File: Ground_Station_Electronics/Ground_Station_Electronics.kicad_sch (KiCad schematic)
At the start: 32 parts

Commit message: "done" but ugly
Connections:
- net SRV1_PWM: now also U2.5 (P3); no longer U2.4 (P2)
- net SRV2_PWM: now also U2.4 (P2); no longer U2.5 (P3)
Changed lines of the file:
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@@
     (effects (font (size 1.27 1.27)) (justify right bottom))
   )
-  (label "SRV1_PWM" (at 63.5 48.26 180)
+  (label "SRV1_PWM" (at 63.5 50.8 180)
     (effects (font (size 1.27 1.27)) (justify right bottom))
   )
@@
     (effects (font (size 1.27 1.27)) (justify left bottom))
   )
-  (label "SRV2_PWM" (at 63.5 50.8 180)
+  (label "SRV2_PWM" (at 63.5 48.26 180)
     (effects (font (size 1.27 1.27)) (justify right bottom))
   )

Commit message: Working on PCB
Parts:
- added H1, H2, H3: MountingHole_Pad, MountingHole:MountingHole_3.2mm_M3_Pad, symbol Mechanical:MountingHole_Pad
- added H4: (no value), symbol Mechanical:MountingHole_Pad
- added J?: (no value), symbol ASTRA_Library:QWIIC_Generic_Conn
- BT1: value (none) -> DNP; footprint (none) -> Connector_AMASS:AMASS_XT30U-M_1x02_P5.0mm_Vertical
- C1, C3: value (none) -> 100u; footprint (none) -> Capacitor_SMD:CP_Elec_10x10
- C2, C5: value (none) -> 1m; footprint (none) -> Capacitor_THT:C_Radial_D10.0mm_H12.5mm_P5.00mm
- C4, C6: value (none) -> 100n; footprint (none) -> Capacitor_SMD:C_0603_1608Metric
- D1, D2, D3: value (none) -> G; footprint (none) -> LED_SMD:LED_0603_1608Metric_Pad1.05x0.95mm_HandSolder
- D4: value (none) -> D_Zener; footprint (none) -> Diode_SMD:D_SMB_Handsoldering
- D5: value (none) -> D_Schottky; footprint (none) -> Diode_SMD:D_SMC_Handsoldering
- F1: value (none) -> Polyfuse; footprint (none) -> Fuse:Fuse_2920_7451Metric_Pad2.10x5.45mm_HandSolder
- J1: value (none) -> RJ45_Shielded_Labelled; footprint (none) -> Connector_RJ:RJ45_Amphenol_RJHSE5380
- J2: value (none) -> ARGB_Header; footprint (none) -> Connector_JST:JST_PH_B3B-PH-K_1x03_P2.00mm_Vertical
- L1: value (none) -> L; footprint (none) -> GS_Library:L_Wuerth_HCF-2920
- M1, M2: value (none) -> Motor_Servo; footprint (none) -> Connector_PinHeader_2.54mm:PinHeader_1x03_P2.54mm_Vertical
- R1: value (none) -> 10; footprint (none) -> Resistor_SMD:R_0603_1608Metric
- R2: value (none) -> 180; footprint (none) -> Resistor_SMD:R_0603_1608Metric
- R3: value (none) -> 3.3k; footprint (none) -> Resistor_SMD:R_0603_1608Metric
- R4, R5: value (none) -> 10k; footprint (none) -> Resistor_SMD:R_0603_1608Metric
- R6, R7: value (none) -> 120; footprint (none) -> Resistor_SMD:R_0603_1608Metric
- U1: value (none) -> LM2576HVS-5; footprint (none) -> Package_TO_SOT_SMD:TO-263-5_TabPin3
- U2: value (none) -> Teensy_4.1; footprint (none) -> ASTRA_Footprints:Teensy4.1
- U3: value (none) -> Adafruit_GPS_V3; footprint (none) -> ASTRA_Footprints:Adafruit_GPS_Breakout
- U4: value (none) -> BNO055_Adafruit_Breakout; footprint (none) -> GS_Library:Adafruit_BNO055
- U5: value (none) -> RFM95W_Adafruit_Breakout; footprint (none) -> ASTRA_Footprints:Adafruit_RFM95W
- U6: value (none) -> MAX3488E; footprint (none) -> Package_SO:SOIC-8_3.9x4.9mm_P1.27mm
- U7: value (none) -> SN74AHCT125D; footprint (none) -> Package_SO:SOIC-14_3.9x8.7mm_P1.27mm
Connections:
- net +3V3: now also J?.2 (3.3V)
- net GND: now also J?.1 (GND)
- net SCL: now also J?.4 (SCL)
- net SDA: now also J?.3 (SDA)

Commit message: schematic save
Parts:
- gave numbers to parts that had none: 1
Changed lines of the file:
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@@
   (symbol (lib_id "power:GND") (at 248.92 88.9 0) (unit 1)
     (in_bom yes) (on_board yes) (fields_autoplaced)
-    (property "Reference" "#PWR?" (id 0) (at 248.92 95.25 0)
+    (property "Reference" "#PWR042" (id 0) (at 248.92 95.25 0)
       (effects (font (size 1.27 1.27)) hide)
     )
@@
   (symbol (lib_id "ASTRA_Library:QWIIC_Generic_Conn") (at 265.43 76.2 0) (unit 1)
     (in_bom yes) (on_board yes) (fields_autoplaced)
-    (property "Reference" "J?" (id 0) (at 269.875 82.9853 0)
+    (property "Reference" "J3" (id 0) (at 269.875 82.9853 0)
       (effects (font (size 1.27 1.27)) (justify left))
     )
@@
   (symbol (lib_id "power:+3.3V") (at 248.92 83.82 0) (unit 1)
     (in_bom yes) (on_board yes) (fields_autoplaced)
-    (property "Reference" "#PWR?" (id 0) (at 248.92 87.63 0)
+    (property "Reference" "#PWR041" (id 0) (at 248.92 87.63 0)
       (effects (font (size 1.27 1.27)) hide)
     )
@@
       (reference "#PWR040") (unit 1) (value "GND") (footprint "")
     )
+    (path "/e92f955a-c3b1-473b-96e0-f304b4f9b568"
+      (reference "#PWR041") (unit 1) (value "+3.3V") (footprint "")
+    )
     (path "/d301b315-959a-46e3-9750-4508835fd0e1"
-      (reference "#PWR?") (unit 1) (value "GND") (footprint "")
-    )
-    (path "/e92f955a-c3b1-473b-96e0-f304b4f9b568"
-      (reference "#PWR?") (unit 1) (value "+3.3V") (footprint "")
+      (reference "#PWR042") (unit 1) (value "GND") (footprint "")
     )
     (path "/9e09a5b2-d433-4c89-b155-f02df3929600"
@@
     )
     (path "/dd409643-2ad0-46ca-8edc-7618874343d8"
-      (reference "J?") (unit 1) (value "QWIIC_Generic_Conn") (footprint "")
+      (reference "J3") (unit 1) (value "QWIIC_Generic_Conn") (footprint "Connector_JST:JST_SH_BM04B-SRSS-TB_1x04-1MP_P1.00mm_Vertical")
     )
     (path "/e4f4697e-5312-4a89-90e5-2b44e8db87d1"

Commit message: Changes
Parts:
- removed H3: MountingHole_Pad, MountingHole:MountingHole_3.2mm_M3_Pad, symbol Mechanical:MountingHole_Pad
- removed H4: (no value), symbol Mechanical:MountingHole_Pad
- H1, H2: value MountingHole_Pad -> (none); footprint MountingHole:MountingHole_3.2mm_M3_Pad -> (none)
- J3: value (none) -> QWIIC_Generic_Conn; footprint (none) -> Connector_JST:JST_SH_BM04B-SRSS-TB_1x04-1MP_P1.00mm_Vertical
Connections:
- net +24V: now also C1.1, D4.1 (K), F1.1, U1.1 (VIN); no longer BT1.2 (Pos), F1.2, J1.5 (~{BLU}), J1.6 (ORG)
- net GND: now also J1.5 (~{BLU}), J1.6 (ORG); no longer J1.3 (~{ORG}), J1.4 (BLU)
- new net Power_in: BT1.2 (Pos), F1.2, J1.3 (~{ORG}), J1.4 (BLU)
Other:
- moved on the sheet: J1

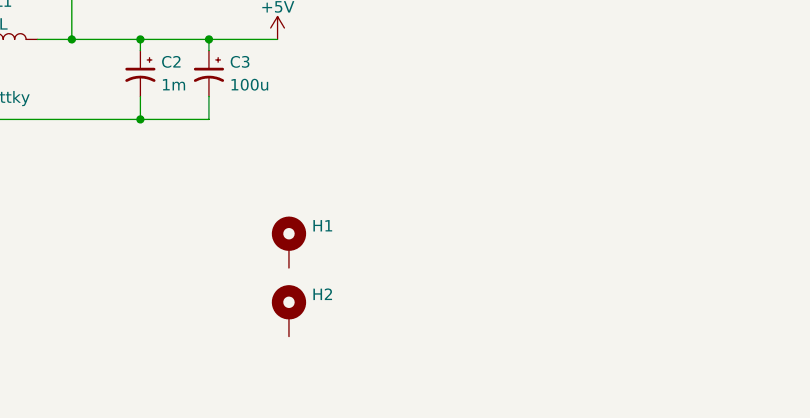
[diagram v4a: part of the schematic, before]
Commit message: Added Dongle
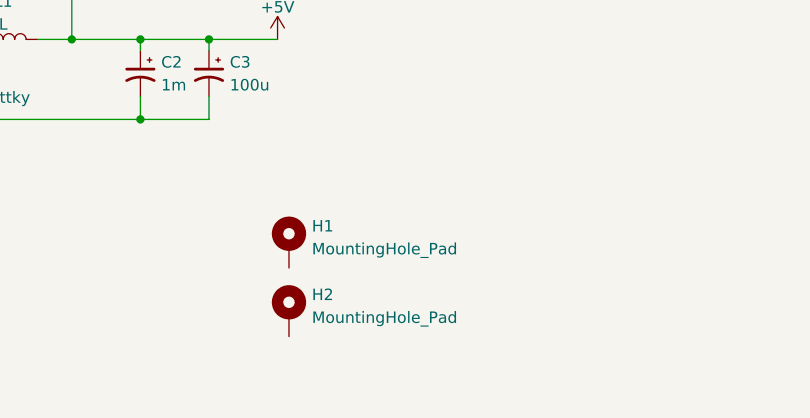
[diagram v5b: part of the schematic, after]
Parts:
- H1, H2: value (none) -> MountingHole_Pad; footprint (none) -> MountingHole:MountingHole_4.3mm_M4_Pad
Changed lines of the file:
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@@
       (effects (font (size 1.27 1.27)) (justify left))
     )
-    (property "Value" "" (id 1) (at 134.62 160.4522 0)
-      (effects (font (size 1.27 1.27)) (justify left))
-    )
-    (property "Footprint" "" (id 2) (at 132.08 160.02 0)
+    (property "Value" "MountingHole_Pad" (id 1) (at 134.62 160.4522 0)
+      (effects (font (size 1.27 1.27)) (justify left))
+    )
+    (property "Footprint" "MountingHole:MountingHole_4.3mm_M4_Pad" (id 2) (at 132.08 160.02 0)
       (effects (font (size 1.27 1.27)) hide)
     )
@@
       (effects (font (size 1.27 1.27)) (justify left))
     )
-    (property "Value" "" (id 1) (at 134.62 168.0722 0)
-      (effects (font (size 1.27 1.27)) (justify left))
-    )
-    (property "Footprint" "" (id 2) (at 132.08 167.64 0)
-      (effects (font (size 1.27 1.27)) hide)
-    )
+    (property "Value" "MountingHole_Pad" (id 1) (at 134.62 168.0722 0)
+      (effects (font (size 1.27 1.27)) (justify left))
+    )
+    (property "Footprint" "MountingHole:MountingHole_4.3mm_M4_Pad" (id 2) (at 132.08 167.64 0)
+      (effects (font (size 1.27 1.27)) hide)
+    )

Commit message: Updated, ready to order
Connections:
- net GND: no longer J1.SH
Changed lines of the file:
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@@
   (junction (at 201.93 109.22) (diameter 0) (color 0 0 0 0)
-  )
-  (junction (at 237.49 138.43) (diameter 0) (color 0 0 0 0)
   )
   (junction (at 107.95 137.16) (diameter 0) (color 0 0 0 0)
@@
     (stroke (width 0) (type default) (color 0 0 0 0))
   )
-  (wire (pts (xy 250.19 137.16) (xy 250.19 138.43))
-    (stroke (width 0) (type default) (color 0 0 0 0))
-  )
   (wire (pts (xy 107.95 137.16) (xy 107.95 129.54))
     (stroke (width 0) (type default) (color 0 0 0 0))
@@
     (stroke (width 0) (type default) (color 0 0 0 0))
   )
-  (wire (pts (xy 237.49 138.43) (xy 234.95 138.43))
-    (stroke (width 0) (type default) (color 0 0 0 0))
-  )
   (wire (pts (xy 71.12 170.18) (xy 73.66 170.18))
     (stroke (width 0) (type default) (color 0 0 0 0))
@@
     (stroke (width 0) (type default) (color 0 0 0 0))
   )
-  (wire (pts (xy 234.95 138.43) (xy 234.95 140.97))
+  (wire (pts (xy 237.49 121.92) (xy 237.49 140.97))
     (stroke (width 0) (type default) (color 0 0 0 0))
   )
@@
     (stroke (width 0) (type default) (color 0 0 0 0))
   )
-  (wire (pts (xy 237.49 121.92) (xy 237.49 138.43))
-    (stroke (width 0) (type default) (color 0 0 0 0))
-  )
   (wire (pts (xy 43.18 146.05) (xy 53.34 146.05))
     (stroke (width 0) (type default) (color 0 0 0 0))
@@
   )
   (wire (pts (xy 55.88 137.16) (xy 53.34 137.16))
-    (stroke (width 0) (type default) (color 0 0 0 0))
-  )
-  (wire (pts (xy 250.19 138.43) (xy 237.49 138.43))
     (stroke (width 0) (type default) (color 0 0 0 0))
   )
@@
     (pin "2")
   )
-  (symbol (lib_id "power:GND") (at 234.95 140.97 0) (unit 1)
-    (in_bom yes) (on_board yes) (fields_autoplaced)
-    (property "Reference" "#PWR035" (id 0) (at 234.95 147.32 0)
-      (effects (font (size 1.27 1.27)) hide)
-    )
-    (property "Value" "GND" (id 1) (at 234.95 145.4134 0))
-    (property "Footprint" "" (id 2) (at 234.95 140.97 0)
-      (effects (font (size 1.27 1.27)) hide)
-    )
-    (property "Datasheet" "" (id 3) (at 234.95 140.97 0)
-      (effects (font (size 1.27 1.27)) hide)
-    )
+  (symbol (lib_id "power:GND") (at 237.49 140.97 0) (unit 1)
+    (in_bom yes) (on_board yes) (fields_autoplaced)
+    (property "Reference" "#PWR035" (id 0) (at 237.49 147.32 0)
+      (effects (font (size 1.27 1.27)) hide)
+    )
+    (property "Value" "GND" (id 1) (at 237.49 145.4134 0))
+    (property "Footprint" "" (id 2) (at 237.49 140.97 0)
+      (effects (font (size 1.27 1.27)) hide)
+    )
+    (property "Datasheet" "" (id 3) (at 237.49 140.97 0)
+      (effects (font (size 1.27 1.27)) hide)
+    )
